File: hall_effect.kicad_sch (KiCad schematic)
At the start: 4 parts, among them U2 MLX90393SLW-ABA-011-RE

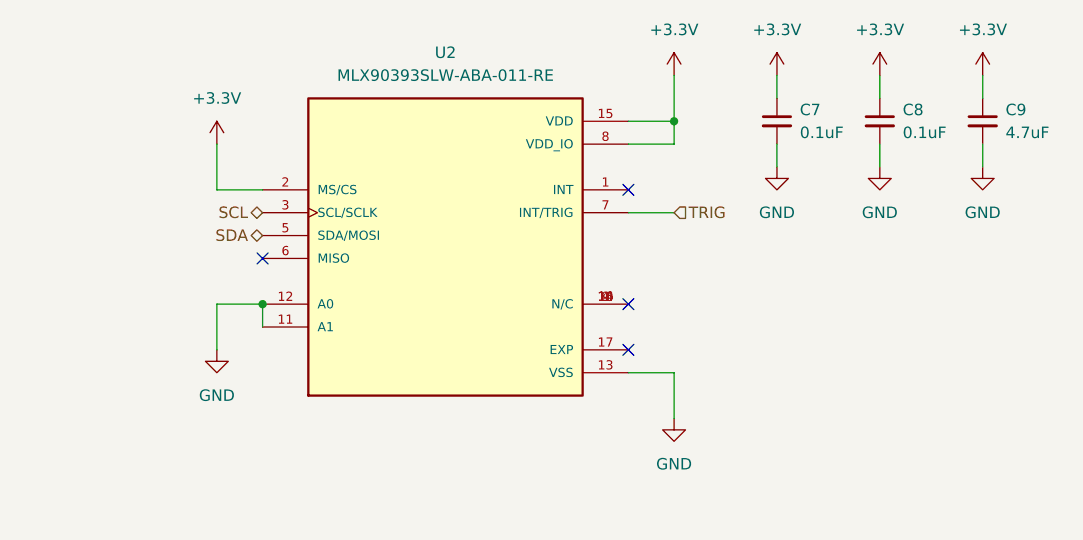
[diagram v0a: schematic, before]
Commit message: Made changes up to diode logic
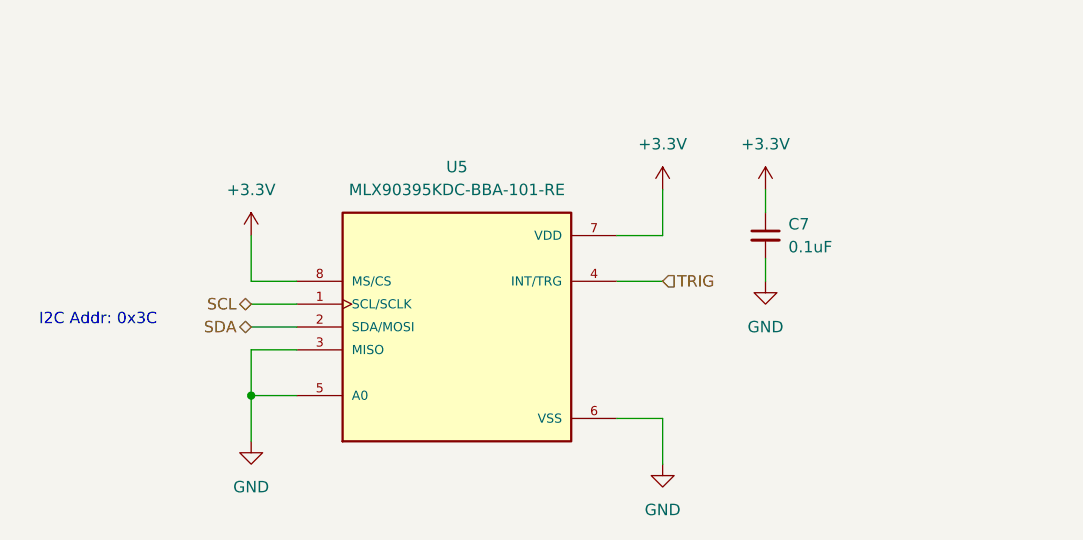
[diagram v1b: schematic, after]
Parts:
- removed C8: 0.1uF, Capacitor_SMD:C_0603_1608Metric_Pad1.08x0.95mm_HandSolder, symbol Device:C_Small
- removed C9: 4.7uF, Capacitor_SMD:C_0603_1608Metric_Pad1.08x0.95mm_HandSolder, symbol Device:C_Small
- removed U2: MLX90393SLW-ABA-011-RE, bookbuddy:QFN50P300X300X100-17N, symbol MLX90393SLW-ABA-011-RE:MLX90393SLW-ABA-011-RE
- added U5: MLX90395KDC-BBA-101-RE, bookbuddy:SOIC127P600X172-8N, symbol MLX90395KDC-BBA-101-RE:MLX90395KDC-BBA-101-RE
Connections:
- net +3.3V: now also U5.7 (VDD), U5.8 (MS/CS)
- net GND: now also U5.3 (MISO), U5.5 (A0), U5.6 (VSS)
- net SCL: now also U5.1 (SCL/SCLK)
- net SDA: now also U5.2 (SDA/MOSI)
- net TRIG: now also U5.4 (INT/TRG)
- no-connect marks 4 -> 0
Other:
- note added: "I2C Addr: 0x3C"
- moved on the sheet: C7

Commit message: addressed Craig's comments
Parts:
- renumbered C7 to C8, U5 to U2
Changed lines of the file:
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@@
 		(dnp no)
 		(fields_autoplaced yes)
-		(property "Reference" "U5"
+		(property "Reference" "U2"
 			(at 134.62 85.09 0)
 			(effects
@@
 			(project ""
 				(path "/5c9eb70e-53a3-4f57-8f37-8853f9cac53c/6dc440b8-7071-4cc1-81fc-db5797234b2d"
-					(reference "U5")
+					(reference "U2")
 					(unit 1)
 				)
@@
 		(dnp no)
 		(fields_autoplaced yes)
-		(property "Reference" "#PWR053"
+		(property "Reference" "#PWR023"
 			(at 157.48 91.44 0)
 			(effects
@@
 			(project ""
 				(path "/5c9eb70e-53a3-4f57-8f37-8853f9cac53c/6dc440b8-7071-4cc1-81fc-db5797234b2d"
-					(reference "#PWR053")
+					(reference "#PWR023")
 					(unit 1)
 				)
@@
 		(dnp no)
 		(fields_autoplaced yes)
-		(property "Reference" "#PWR054"
+		(property "Reference" "#PWR024"
 			(at 157.48 124.46 0)
 			(effects
@@
 			(project "bookbuddy_pcb"
 				(path "/5c9eb70e-53a3-4f57-8f37-8853f9cac53c/6dc440b8-7071-4cc1-81fc-db5797234b2d"
-					(reference "#PWR054")
+					(reference "#PWR024")
 					(unit 1)
 				)
@@
 		(dnp no)
 		(fields_autoplaced yes)
-		(property "Reference" "#PWR022"
+		(property "Reference" "#PWR026"
 			(at 168.91 104.14 0)
 			(effects
@@
 			(project "bookbuddy_pcb"
 				(path "/5c9eb70e-53a3-4f57-8f37-8853f9cac53c/6dc440b8-7071-4cc1-81fc-db5797234b2d"
-					(reference "#PWR022")
+					(reference "#PWR026")
 					(unit 1)
 				)
@@
 		(dnp no)
 		(fields_autoplaced yes)
-		(property "Reference" "C7"
+		(property "Reference" "C8"
 			(at 171.45 91.4462 0)
 			(effects
@@
 			(project ""
 				(path "/5c9eb70e-53a3-4f57-8f37-8853f9cac53c/6dc440b8-7071-4cc1-81fc-db5797234b2d"
-					(reference "C7")
+					(reference "C8")
 					(unit 1)
 				)
@@
 		(dnp no)
 		(fields_autoplaced yes)
-		(property "Reference" "#PWR056"
+		(property "Reference" "#PWR021"
 			(at 111.76 96.52 0)
 			(effects
@@
 			(project "bookbuddy_pcb"
 				(path "/5c9eb70e-53a3-4f57-8f37-8853f9cac53c/6dc440b8-7071-4cc1-81fc-db5797234b2d"
-					(reference "#PWR056")
+					(reference "#PWR021")
 					(unit 1)
 				)
@@
 		(dnp no)
 		(fields_autoplaced yes)
-		(property "Reference" "#PWR055"
+		(property "Reference" "#PWR022"
 			(at 111.76 121.92 0)
 			(effects
@@
 			(project "bookbuddy_pcb"
 				(path "/5c9eb70e-53a3-4f57-8f37-8853f9cac53c/6dc440b8-7071-4cc1-81fc-db5797234b2d"
-					(reference "#PWR055")
+					(reference "#PWR022")
 					(unit 1)
 				)
@@
 		(dnp no)
 		(fields_autoplaced yes)
-		(property "Reference" "#PWR021"
+		(property "Reference" "#PWR025"
 			(at 168.91 91.44 0)
 			(effects
@@
 			(project "bookbuddy_pcb"
 				(path "/5c9eb70e-53a3-4f57-8f37-8853f9cac53c/6dc440b8-7071-4cc1-81fc-db5797234b2d"
-					(reference "#PWR021")
-					(unit 1)
-				)
+					(reference "#PWR025")
+					(unit 1)
+				)
